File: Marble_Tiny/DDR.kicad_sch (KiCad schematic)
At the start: 55 parts, among them U2 AS4C256M16D3

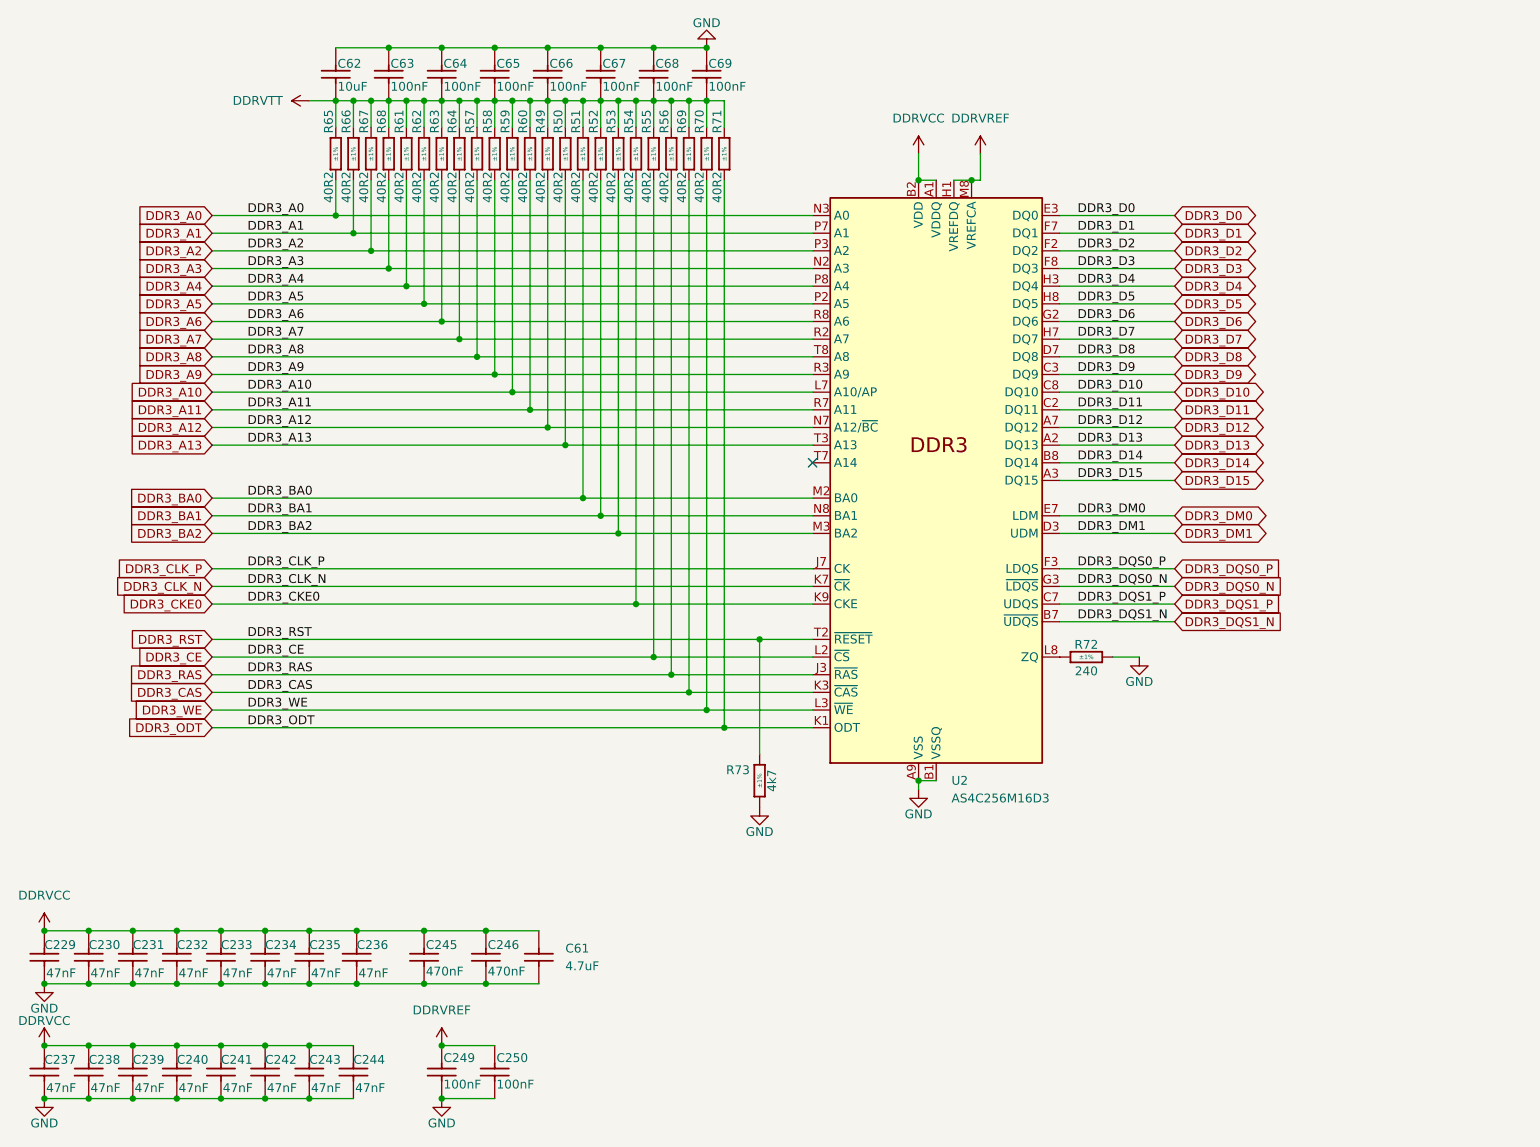
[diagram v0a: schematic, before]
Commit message: connected more address lines to DDR, new board name
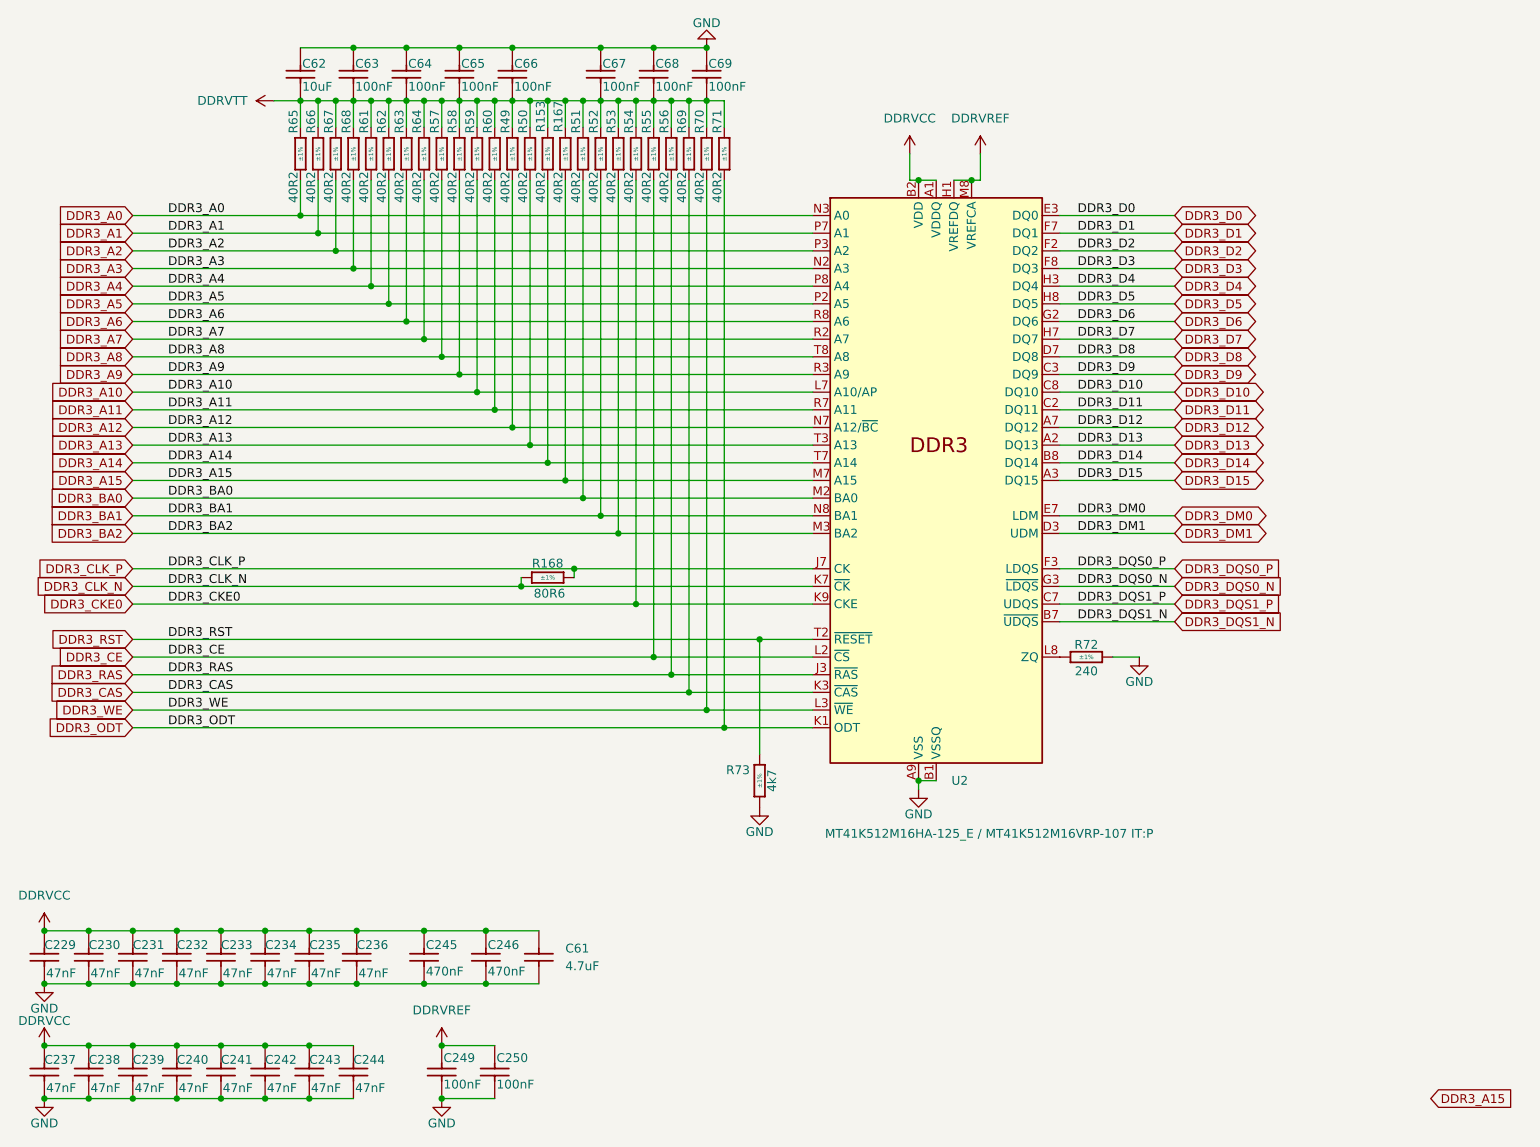
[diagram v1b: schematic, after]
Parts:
- added R153, R167: R0402_40R2_1%_0.0625W_100PPM, Resistors SMD:RESC1005X40N, symbol Resistors SMD:R0402_40R2_1%_0.0625W_100PPM
- added R168: R0402_80R6_1%_0.1W_100PPM, Resistors SMD:RESC1005X40N, symbol Resistors SMD:R0402_80R6_1%_0.1W_100PPM
- U2: value AS4C256M16D3 -> MT41K512M16HA-125_E / MT41K512M16VRP-107 IT:P; footprint Package_BGA:BGA-96_9.0x13.0mm_Layout2x3x16_P0.8mm -> Package_BGA:FBGA-96_9x14mm_Layout9x16_P0.8mm
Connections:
- net DDR3_CLK_N: now also R168.1
- net DDR3_CLK_P: now also R168.2
- net DDRVTT: now also R153.2, R167.2
- net DDR3_A15: now reaches U2.M7 (A15)
- net DDR3_A15: now also R167.1
- net DDR3_A14: now reaches U2.T7 (A14)
- net DDR3_A14: now also R153.1
- no-connect marks 1 -> 0
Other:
- moved on the sheet: C62, C63, C64, C65, C66, R49, R50, R57, R58, R59, R60, R61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
